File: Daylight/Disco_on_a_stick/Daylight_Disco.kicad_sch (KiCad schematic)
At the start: 38 parts, among them J1 Conn_01x03_Male, J2 Conn_01x01_Male, J3 Conn_01x01_Male

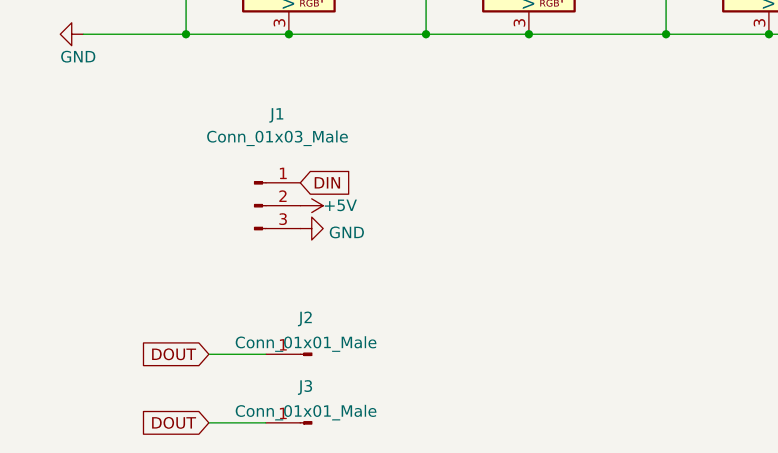
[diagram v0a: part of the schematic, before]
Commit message: Daylight | Add output connectors to the RGB sticks
Provided pick and place files for all varieties as well.
Created individual README.md files with BOM and changelog.
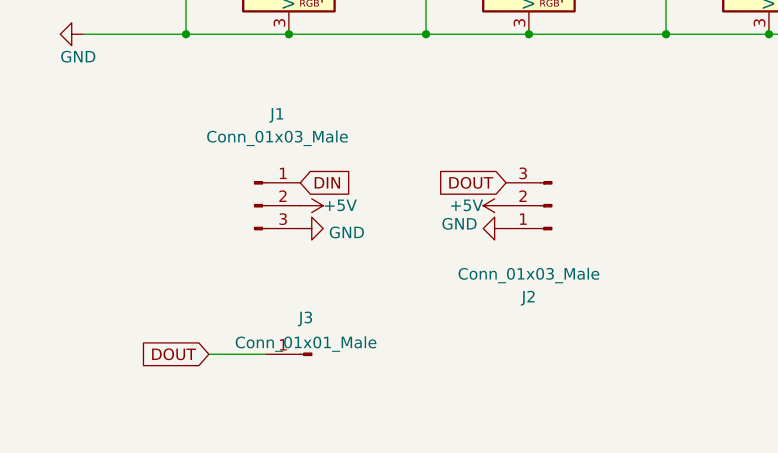
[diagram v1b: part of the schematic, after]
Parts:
- removed J2: Conn_01x01_Male, Daylight:PinHeader-1-with-SMDpad, symbol Connector:Conn_01x01_Male
- added J2: Conn_01x03_Male, Daylight:JST_XH_S3B-XH-A-1_1x03_P2.50mm_Horizontal, symbol Connector:Conn_01x03_Male
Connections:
- net +5V: now also J2.2 (Pin_2)
- net DOUT: now also J2.3 (Pin_3)
- net GND: now also J2.1 (Pin_1)
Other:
- moved on the sheet: J3
